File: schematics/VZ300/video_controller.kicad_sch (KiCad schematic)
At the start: 15 parts, among them U15 MC6847, U16 6116

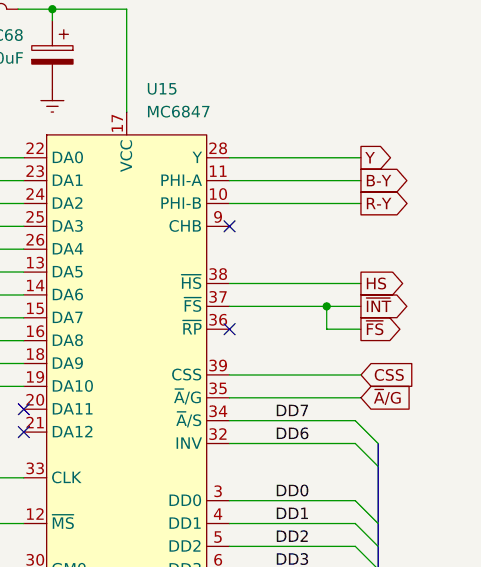
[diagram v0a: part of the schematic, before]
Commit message: Fix some minor issues in the VZ300 schematic
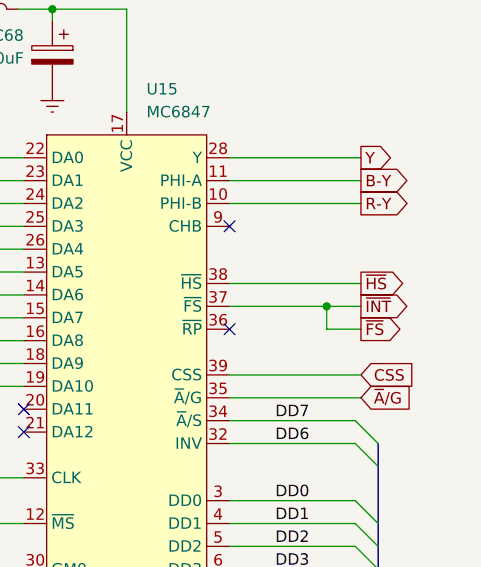
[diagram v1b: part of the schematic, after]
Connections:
- net HS renamed ~{HS}
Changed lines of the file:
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@@
     )
   )
-  (global_label "HS" (shape output) (at 227.33 73.025 0) (fields_autoplaced)
+  (global_label "~{HS}" (shape output) (at 227.33 73.025 0) (fields_autoplaced)
     (effects (font (size 1.27 1.27)) (justify left))
     (property "Intersheetrefs" "${INTERSHEET_REFS}" (at 232.8552 73.025 0)
